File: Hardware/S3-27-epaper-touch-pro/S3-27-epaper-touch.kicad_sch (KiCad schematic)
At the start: 102 parts, among them J1 AFC24-S24FIC-00, J10 Conn_01x06_Pin, J2 Conn_01x06, J3 Conn_01x06, J4 TochConn, J5 Groove sensor, J6 Conn_01x05_Pin, J7 Conn_01x04_Pin, J8 Conn_01x06, Q1 Si1308, Q2 Si2301, SW1 SW_Push, SW2 SW_Push, SW3 SW_Push, SW4 SW_Push, SW5 SW_Push, SW6 SW_Push, SW7 SW_Push, SW8 SW_Push, SW9 SW_Push, U1 ESP32-S3-WROOM-1-N8, U2 RT9013, U3 KoreanHropartsElecTYPE-C-31-M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, U5 BME680, U6 TPL5110, U7 RFM95W-868S2, U8 LSM6DSL

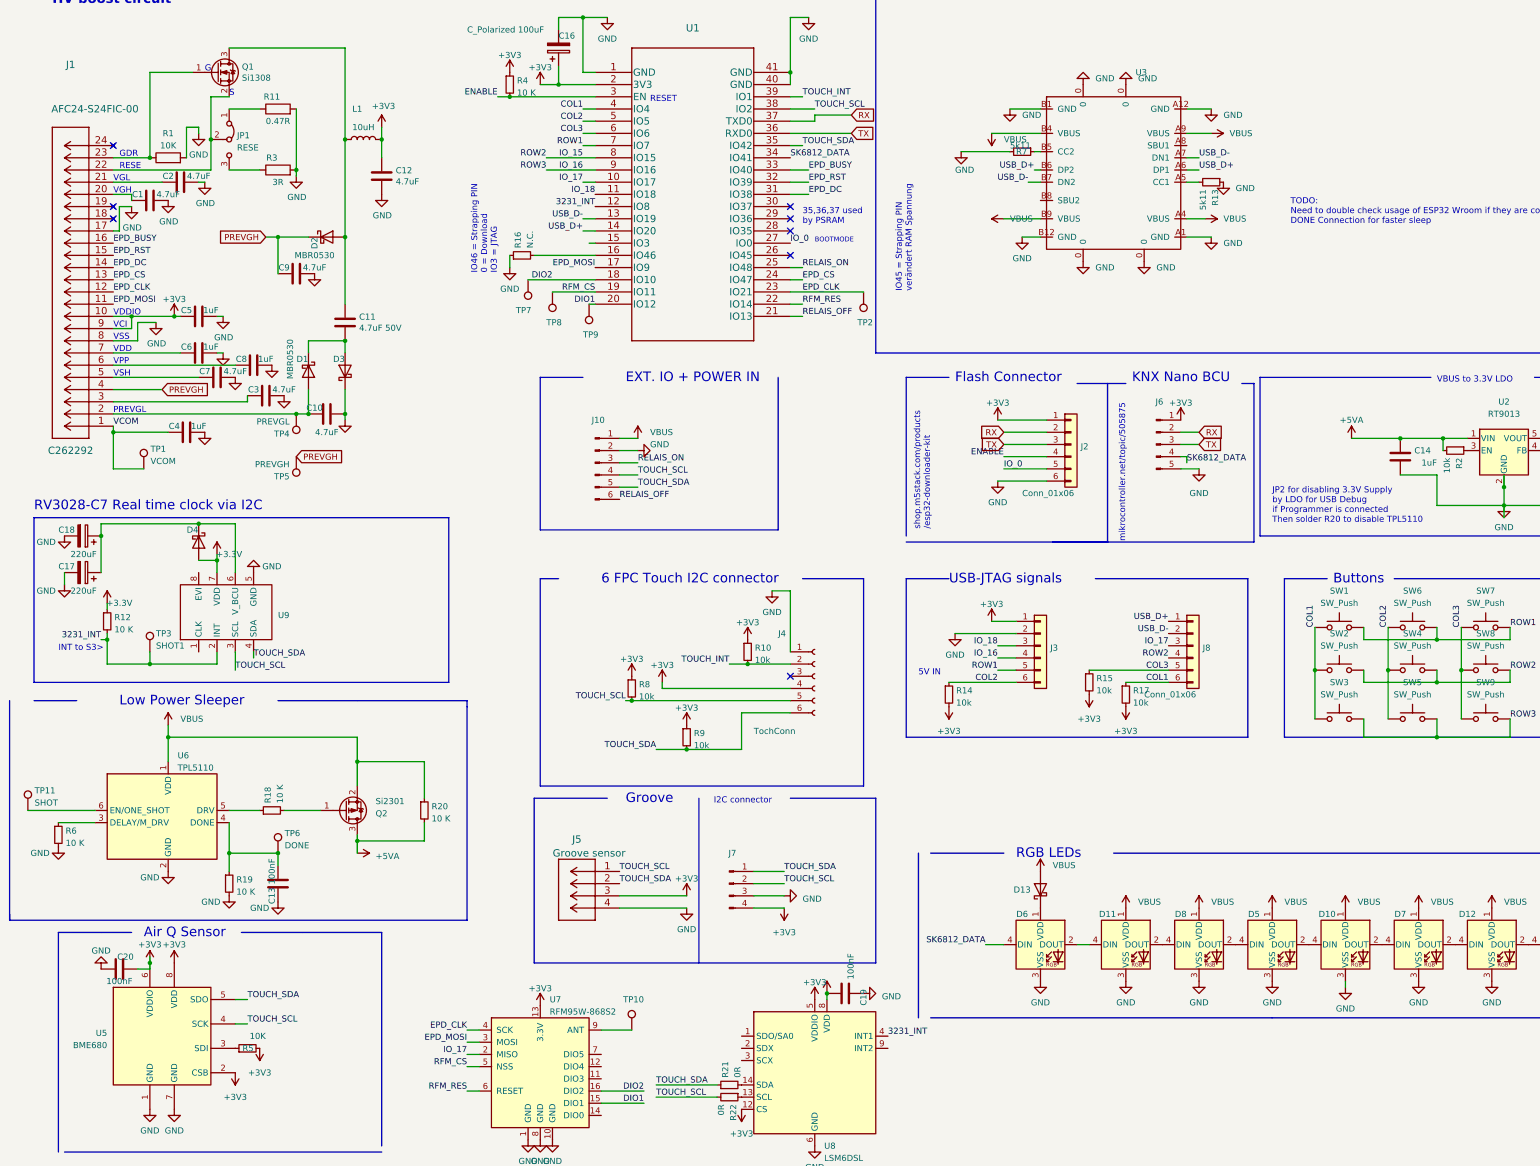
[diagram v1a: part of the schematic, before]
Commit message: Found a wiring Bug on the BME680
SDA had no pinning
wired several other lines with bigger lines
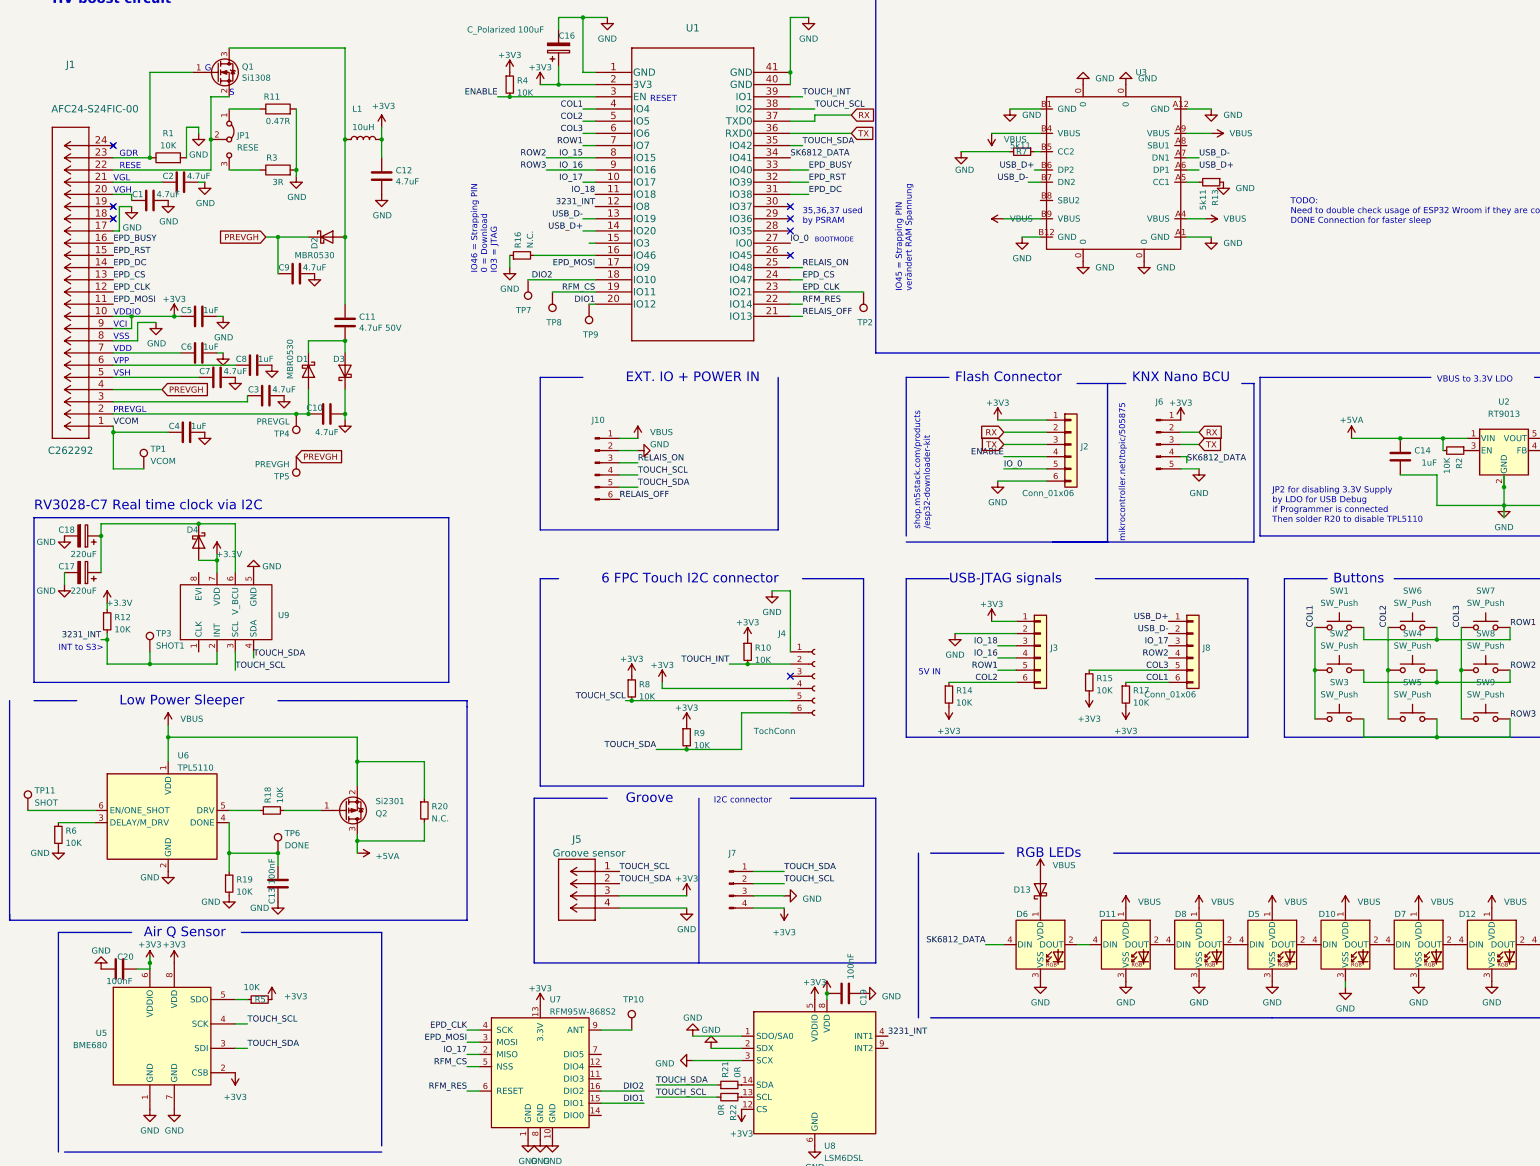
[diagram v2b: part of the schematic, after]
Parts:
- C1, C10, C12, C2, C3, C7, C9: LCSC C1779 -> C162420
- C11: LCSC C28323 -> C162420
- C17, C18: LCSC C122252 -> (none)
- D1, D13, D2, D3, D4: LCSC C77336 -> (none)
- D10, D11, D12, D5, D6, D7, D8, D9: LCSC C5149201 -> (none)
- J1: LCSC (none) -> C262292
- JP1: LCSC (none) -> C2911519
- L1: LCSC C38117 -> (none)
- Q1: LCSC C469327 -> (none)
- R1: LCSC (none) -> C17414
- R10, R14, R15, R17, R2, R8, R9: value 10k -> 10K
- R12, R18, R19, R4, R6: value 10 K -> 10K
- R16: LCSC C25804 -> (none)
- R20: value 10 K -> N.C.; LCSC C17414 -> (none)
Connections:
- net GND: now also U8.1 (SDO/SA0), U8.2 (SDX), U8.3 (SCX)
- net TOUCH_SDA: now also U5.3 (SDI); no longer U5.5 (SDO)
- net at R5.1: now also U5.5 (SDO); no longer U5.3 (SDI)
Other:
- moved on the sheet: R5

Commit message: Add files via upload
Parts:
- added R23: LDR03, OptoDevice:R_LDR_10x8.5mm_P7.6mm_Vertical, symbol Sensor_Optical:LDR03
- added R24: N.C., Resistor_SMD:R_0805_2012Metric_Pad1.20x1.40mm_HandSolder, symbol Device:R_Small
- C1, C2, C3, C7: value 4.7uF -> 1uF; LCSC C162420 -> C28323
- C10: value 4.7uF -> 4.7uF 50V_US
- C11: value 4.7uF 50V -> 4.7uF 50V_US
- C12, C9: value 4.7uF -> 4.7uF 50V US
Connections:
- net GND: now also R24.2
- net IO_18: now also R23.2, R24.1
- net VBUS: now also R23.1
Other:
- note added: "I²C Address - 0x52 RV3028 - 0xD4/D6 LSM6DSL - 0x77 BME"
- note added: "Light Sensor"
- note added: "TODO: - 3231_INT ist verbunden mit LSM6DSL, RV3028. sinnvoll? - USB ESD Diodes"
- note removed: "HV boost circuit"
- note removed: "INT to S3>"
- note removed: "TODO: - USB ESD Diodes - RV3028 einbauen - überlegen ob 220uF Kondensatoren Sinn machen oder Ladestrom gebrenzt werden muss"
- note removed: "TODO: Need to double check usage of ESP32 Wroom if they are compatible to current pinning DONE Connection for faster sleep"
- moved on the sheet: C17, C18, TP11

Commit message: Add files via upload
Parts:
- removed R20: N.C., Resistor_SMD:R_0805_2012Metric_Pad1.20x1.40mm_HandSolder, symbol Device:R_Small
- added JP3, JP5: Jumper_2_Bridged, Jumper:SolderJumper-2_P1.3mm_Bridged_RoundedPad1.0x1.5mm, symbol Jumper:Jumper_2_Bridged
- added JP4: Jumper_2_Open, Jumper:SolderJumper-2_P1.3mm_Open_RoundedPad1.0x1.5mm, symbol Jumper:Jumper_2_Open
- added TP12, TP13: VCOM, TestPoint:TestPoint_Pad_D1.5mm, symbol Connector:TestPoint
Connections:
- net +5VA: now also JP4.2 (B)
- net 3231_INT: now also JP3.2 (B), JP5.1 (A); no longer U8.4 (INT1), U9.2 (INT)
- net VBUS: now also JP4.1 (A)
- net at U8.9 (INT2): now also TP12.1
- new net: JP5.2 (B), U9.2 (INT)
- new net: JP3.1 (A), TP13.1, U8.4 (INT1)
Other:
- note added: "Jumper: - JP2 = If USB Power Connected and 3.3V Programmer - JP3 = GYRO INT Emergency CUT - JP4 = MAINS Mode / No TPL5110 Mode - JP5 = RV3028 INT Emergency CUT"
- note added: "Testpoints: - TP1 EPD VCOM - TP2 EPD CLK - TP3 INT RV3028 - TP4 EPD PREVGL - TP5 EPD PREVGH - TP6 TPL5110 DONE - TP7 RFM DIO2 - TP8 RFM CS - TP9 RFM DIO1 - TP10 RFM ANT - TP11 TPL5110 SHOT - TP12 GYRO INT2 - TP13 GYRO INT1"

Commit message: Add files via upload
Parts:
- added H6: MountingSwitch, MountingHole:MountingHole_3.2mm_M3, symbol Mechanical:MountingHole
- added R20: 100R, Resistor_SMD:R_0805_2012Metric_Pad1.20x1.40mm_HandSolder, symbol Device:R_Small
- added TP14: RESET_TOUCH, TestPoint:TestPoint_Pad_D1.5mm, symbol Connector:TestPoint
- C12, C9: value 4.7uF 50V US -> 4.7uF 50V_US
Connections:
- net at C17.1, C18.1, U9.6 (V_BCU): now also R20.2; no longer D4.1 (K)
- net at J4.3 (Pin_3): now also TP14.1
- new net: D4.1 (K), R20.1
- no-connect marks 8 -> 7
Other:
- note added: "Jumper: - JP2 = OPEN if USB Power Connected and 3.3V Programmer - JP3 = GYRO INT Emergency CUT - JP4 = MAINS Mode / No TPL5110 Mode - JP5 = RV3028 INT Emergency CUT"
- note removed: "Jumper: - JP2 = If USB Power Connected and 3.3V Programmer - JP3 = GYRO INT Emergency CUT - JP4 = MAINS Mode / No TPL5110 Mode - JP5 = RV3028 INT Emergency CUT"
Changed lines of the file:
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@@
   (junction (at 116.84 68.58) (diameter 0) (color 0 0 0 0)
   )
-  (junction (at 78.74 148.59) (diameter 0) (color 0 0 0 0)
-  )
   (junction (at 99.06 125.73) (diameter 0) (color 0 0 0 0)
   )
@@
   (junction (at 73.66 105.41) (diameter 0) (color 0 0 0 0)
   )
+  (junction (at 69.85 148.59) (diameter 0) (color 0 0 0 0)
+  )
   (junction (at 337.82 130.81) (diameter 0) (color 0 0 0 0)
   )
@@
   (junction (at 193.04 177.8) (diameter 0) (color 0 0 0 0)
   )
-  (junction (at 69.85 148.59) (diameter 0) (color 0 0 0 0)
-  )
   (junction (at 361.95 130.81) (diameter 0) (color 0 0 0 0)
   )
@@
   (no_connect (at 60.96 82.55))
   (no_connect (at 201.93 82.55))
-  (no_connect (at 201.93 180.34))
   (no_connect (at 201.93 87.63))
   (polyline (pts (xy 379.73 118.11) (xy 379.73 151.13))
@@
     (stroke (width 0) (type default))
   )
+  (wire (pts (xy 76.2 148.59) (xy 78.74 148.59))
+    (stroke (width 0) (type default))
+  )
   (polyline (pts (xy 44.45 147.32) (xy 130.81 147.32))
     (stroke (width 0) (type default))
@@
     (stroke (width 0) (type default))
   )
+  (wire (pts (xy 69.85 148.59) (xy 69.85 147.32))
+    (stroke (width 0) (type default))
+  )
   (wire (pts (xy 364.49 130.81) (xy 361.95 130.81))
     (stroke (width 0) (type default))
@@
     (stroke (width 0) (type default))
   )
+  (wire (pts (xy 177.8 175.26) (xy 177.8 180.34))
+    (stroke (width 0) (type default))
+  )
   (polyline (pts (xy 381 160.02) (xy 375.92 160.02))
     (stroke (width 0) (type default))
@@
     (stroke (width 0) (type default))
   )
-  (wire (pts (xy 78.74 148.59) (xy 86.36 148.59))
-    (stroke (width 0) (type default))
-  )
   (polyline (pts (xy 375.92 160.02) (xy 327.66 160.02))
     (stroke (width 0) (type default))
@@
     (stroke (width 0) (type default))
   )
-  (wire (pts (xy 69.85 148.59) (xy 78.74 148.59))
-    (stroke (width 0) (type default))
-  )
   (polyline (pts (xy 226.06 160.02) (xy 226.06 193.04))
     (stroke (width 0) (type default))
@@
     (stroke (width 0) (type default))
   )
+  (wire (pts (xy 69.85 147.32) (xy 86.36 147.32))
+    (stroke (width 0) (type default))
+  )
   (wire (pts (xy 60.96 115.57) (xy 86.36 115.57))
     (stroke (width 0) (type default))
@@
     (stroke (width 0) (type default))
   )
-  (wire (pts (xy 86.36 148.59) (xy 86.36 158.75))
+  (wire (pts (xy 86.36 147.32) (xy 86.36 158.75))
     (stroke (width 0) (type default))
   )
@@
     (stroke (width 0) (type default))
   )
+  (wire (pts (xy 69.85 148.59) (xy 71.12 148.59))
+    (stroke (width 0) (type default))
+  )
   (wire (pts (xy 201.93 95.25) (xy 204.47 95.25))
     (stroke (width 0) (type default))
@@
     (stroke (width 0) (type default))
   )
+  (wire (pts (xy 177.8 180.34) (xy 201.93 180.34))
+    (stroke (width 0) (type default))
+  )
   (wire (pts (xy 134.62 259.08) (xy 137.16 259.08))
     (stroke (width 0) (type default))
@@
     (effects (font (size 1.27 1.27)) (justify left bottom))
   )
-  (text "Jumper:\n- JP2 = If USB Power Connected and 3.3V Programmer\n- JP3 = GYRO INT Emergency CUT\n- JP4 = MAINS Mode / No TPL5110 Mode\n- JP5 = RV3028 INT Emergency CUT"
+  (text "Jumper:\n- JP2 = OPEN if USB Power Connected and 3.3V Programmer\n- JP3 = GYRO INT Emergency CUT\n- JP4 = MAINS Mode / No TPL5110 Mode\n- JP5 = RV3028 INT Emergency CUT"
     (at 323.85 41.91 0)
     (effects (font (size 1.27 1.27)) (justify left bottom))
@@
       (effects (font (size 1.27 1.27)))
     )
-    (property "Value" "4.7uF 50V US" (at 100.33 100.33 90)
+    (property "Value" "4.7uF 50V_US" (at 100.33 100.33 90)
       (effects (font (size 1.27 1.27)))
     )
@@
       (effects (font (size 1.27 1.27)) (justify left))
     )
-    (property "Value" "220uF" (at 73.66 154.94 90)
-      (effects (font (size 1.27 1.27)) (justify left))
+    (property "Value" "220uF" (at 53.34 154.94 90)
+      (effects (font (size 1.27 1.27)) (justify left) hide)
     )
     (property "Footprint" "Capacitor_Tantalum_SMD:CP_EIA-3528-21_Kemet-B" (at 68.8848 156.21 0)
@@
     )
   )
+  (symbol (lib_id "Connector:TestPoint") (at 177.8 175.26 0) (unit 1)
+    (in_bom yes) (on_board yes) (dnp no)
+    (property "Reference" "TP14" (at 175.26 167.64 0)
+      (effects (font (size 1.27 1.27)) (justify left))
+    )
+    (property "Value" "RESET_TOUCH" (at 171.45 170.18 0)
+      (effects (font (size 1.27 1.27)) (justify left))
+    )
+    (property "Footprint" "TestPoint:TestPoint_Pad_D1.5mm" (at 182.88 175.26 0)
+      (effects (font (size 1.27 1.27)) hide)
+    )
+    (property "Datasheet" "~" (at 182.88 175.26 0)
+      (effects (font (size 1.27 1.27)) hide)
+    )
+    (pin "1")
+    (instances
+      (project "S3-27-epaper-touch"
+        (path "/42575459-fa0a-4761-8328-0238c17cbdda"
+          (reference "TP14") (unit 1)
+        )
+      )
+    )
+  )
   (symbol (lib_id "Mechanical:MountingHole") (at 383.54 26.67 0) (unit 1)
     (in_bom yes) (on_board yes) (dnp no) (fields_autoplaced)
@@
       (effects (font (size 1.27 1.27)) (justify right))
     )
-    (property "Value" "4.7uF 50V US" (at 119.761 77.343 0)
+    (property "Value" "4.7uF 50V_US" (at 119.761 77.343 0)
       (effects (font (size 1.27 1.27)) (justify right))
     )
@@
     )
   )
+  (symbol (lib_id "Device:R_Small") (at 73.66 148.59 270) (unit 1)
+    (in_bom yes) (on_board yes) (dnp no)
+    (property "Reference" "R20" (at 76.2 149.86 0)
+      (effects (font (size 1.27 1.27)) (justify left))
+    )
+    (property "Value" "100R" (at 73.66 149.86 0)
+      (effects (font (size 1.27 1.27)) (justify left))
+    )
+    (property "Footprint" "Resistor_SMD:R_0805_2012Metric_Pad1.20x1.40mm_HandSolder" (at 73.66 148.59 0)
+      (effects (font (size 1.27 1.27)) hide)
+    )
+    (property "Datasheet" "https://datasheet.lcsc.com/lcsc/2206010045_UNI-ROYAL-Uniroyal-Elec-0603WAF1002T5E_C25804.pdf" (at 73.66 148.59 0)
+      (effects (font (size 1.27 1.27)) hide)
+    )
+    (property "LCSC" "" (at 73.66 148.59 0)
+      (effects (font (size 1.27 1.27)) hide)
+    )
+    (pin "1")
+    (pin "2")
+    (instances
+      (project "S3-27-epaper-touch"
+        (path "/42575459-fa0a-4761-8328-0238c17cbdda"
+          (reference "R20") (unit 1)
+        )
+      )
+    )
+  )
   (symbol (lib_id "Sensor_Motion:LSM6DSL") (at 207.01 262.89 0) (unit 1)
     (in_bom yes) (on_board yes) (dnp no) (fields_autoplaced)
@@
         )
       )
+    )
+  )
+  (symbol (lib_id "Mechanical:MountingHole") (at 382.27 74.93 0) (unit 1)
+    (in_bom yes) (on_board yes) (dnp no) (fields_autoplaced)
+    (property "Reference" "H6" (at 384.81 74.0953 0)
+      (effects (font (size 1.27 1.27)) (justify left))
+    )
+    (property "Value" "MountingSwitch" (at 384.81 76.6322 0)
+      (effects (font (size 1.27 1.27)) (justify left))
+    )
+    (property "Footprint" "MountingHole:MountingHole_3.2mm_M3" (at 382.27 74.93 0)
+      (effects (font (size 1.27 1.27)) hide)
+    )
+    (property "Datasheet" "~" (at 382.27 74.93 0)
+      (effects (font (size 1.27 1.27)) hide)
+    )
+    (instances
+      (project "S3-27-epaper-touch"
+        (path "/42575459-fa0a-4761-8328-0238c17cbdda"
+          (reference "H6") (unit 1)
+        )
+      )
